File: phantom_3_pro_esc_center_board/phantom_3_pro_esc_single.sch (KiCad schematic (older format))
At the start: 103 parts

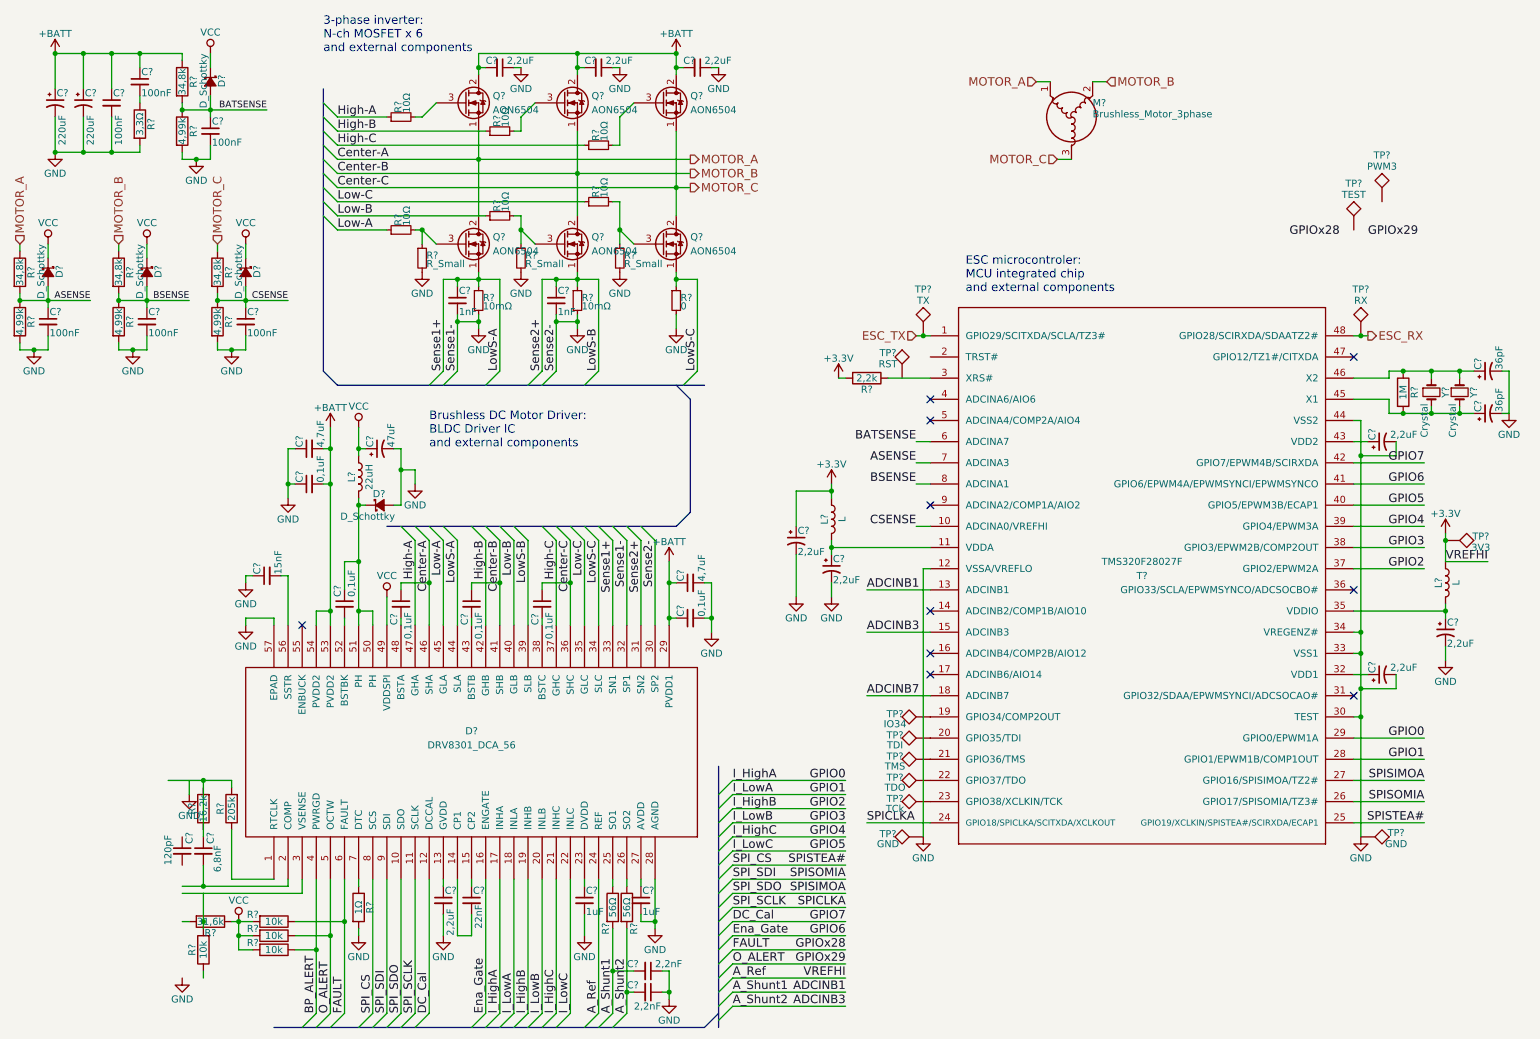
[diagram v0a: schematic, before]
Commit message: Renumbered components.
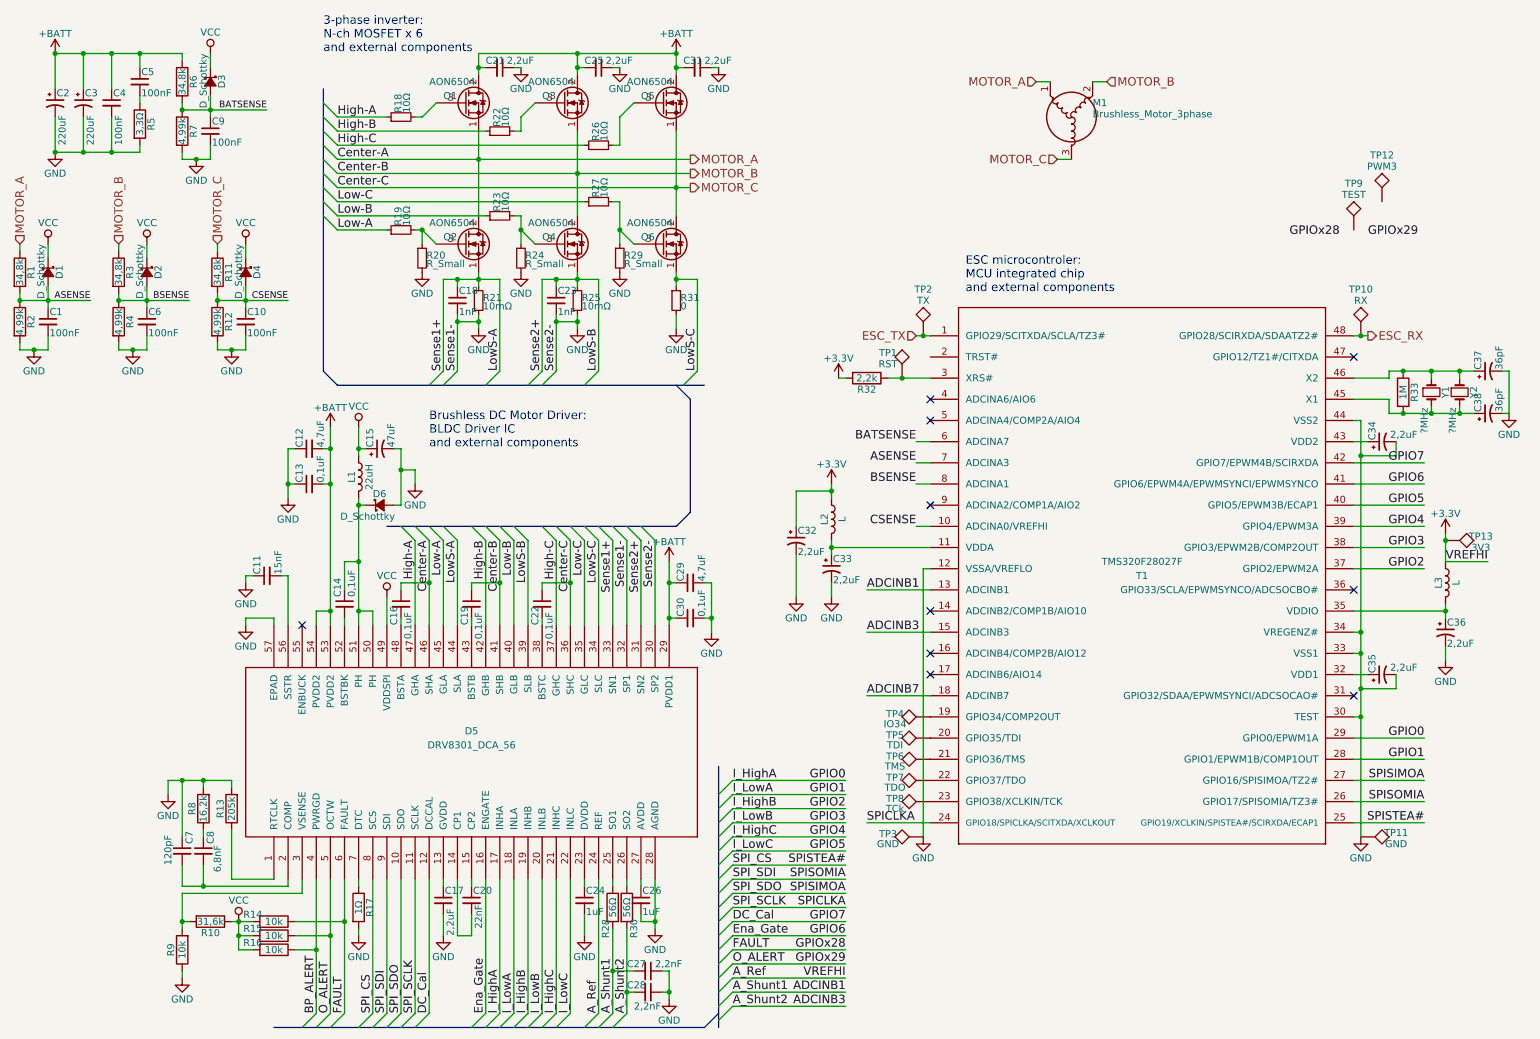
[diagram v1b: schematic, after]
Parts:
- Y3, Y4: renamed from Y?; value Crystal -> ?MHz
- gave numbers to parts that had none: 101
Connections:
- net GND: now also C45.1, R41.2, R42.1, R46.2
- net at C46.2, D11.2 (COMP): now also C45.2
- net at D11.3 (VSENSE): now also R42.2, R43.2
- net at C46.1: now also R41.1; no longer R46.2
- net at R65.1, T2.3 (XRS#): now also TP14.1
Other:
- moved on the sheet: R9

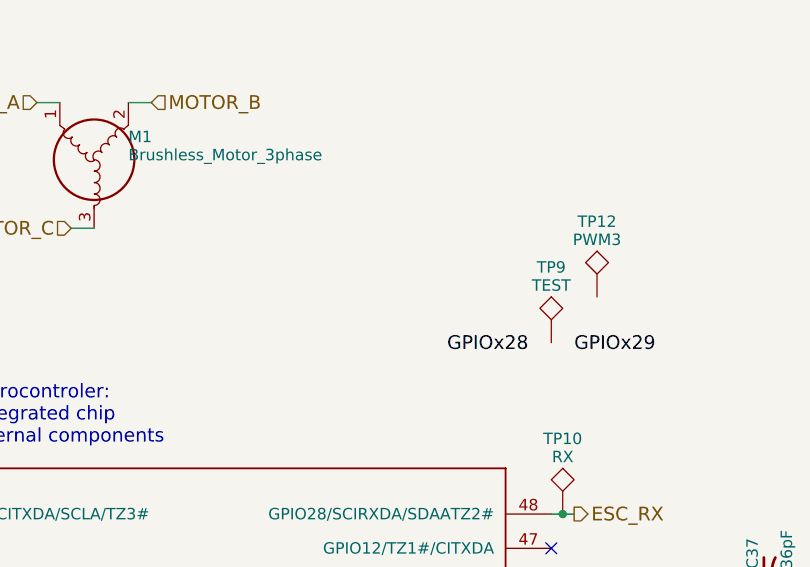
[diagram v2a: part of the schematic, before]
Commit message: ESC Center: Identified pins of FC connection.
Named all FC pins, and linked with proper connectors.
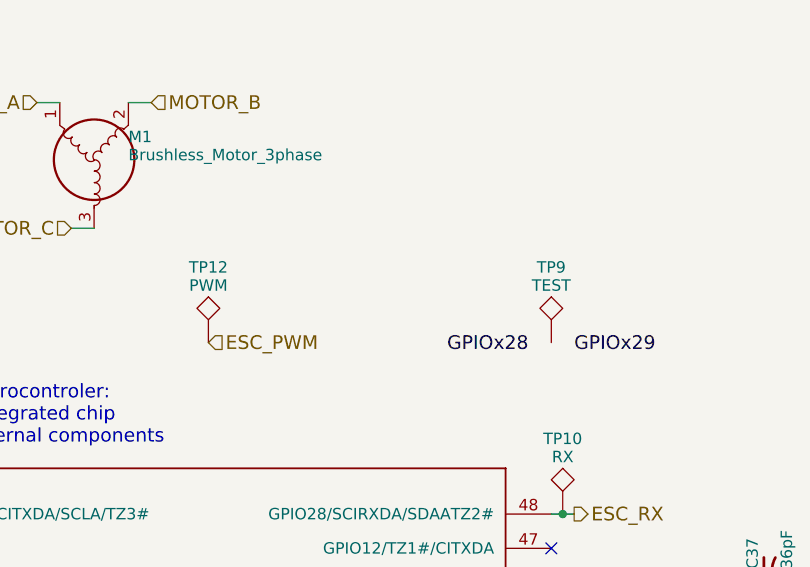
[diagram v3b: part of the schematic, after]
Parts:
- TP25: value PWM3 -> PWM
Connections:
- net ESC_PWM: now reaches TP25.1
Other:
- moved on the sheet: TP12
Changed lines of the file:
@@
 L TEST TP25
 U 1 1 590A73FE
-P 10200 1850
+P 8500 2050
 AR Path="/58FDD387/590A73FE" Ref="TP25"  Part="1"
 AR Path="/58FDAEFB/590A73FE" Ref="TP12"  Part="1"
 AR Path="/58FDDC64/590A73FE" Ref="TP38"  Part="1"
 AR Path="/58FDDC6B/590A73FE" Ref="TP51"  Part="1"
-F 0 "TP12" H 10200 2150 50  0000 C BNN
-F 1 "PWM3" H 10200 2100 50  0000 C CNN
-F 2 "" H 10200 1850 50  0001 C CNN
-F 3 "" H 10200 1850 50  0001 C CNN
-	1    10200 1850
+F 0 "TP12" H 8500 2350 50  0000 C BNN
+F 1 "PWM" H 8500 2300 50  0000 C CNN
+F 2 "" H 8500 2050 50  0001 C CNN
+F 3 "" H 8500 2050 50  0001 C CNN
+	1    8500 2050
 	1    0    0    -1
 $EndComp
@@
 	1700 6700 1700 6550
 Connection ~ 6800 3100
+Text HLabel 8500 2050 2    60   Input ~ 0
+ESC_PWM
 $EndSCHEMATC

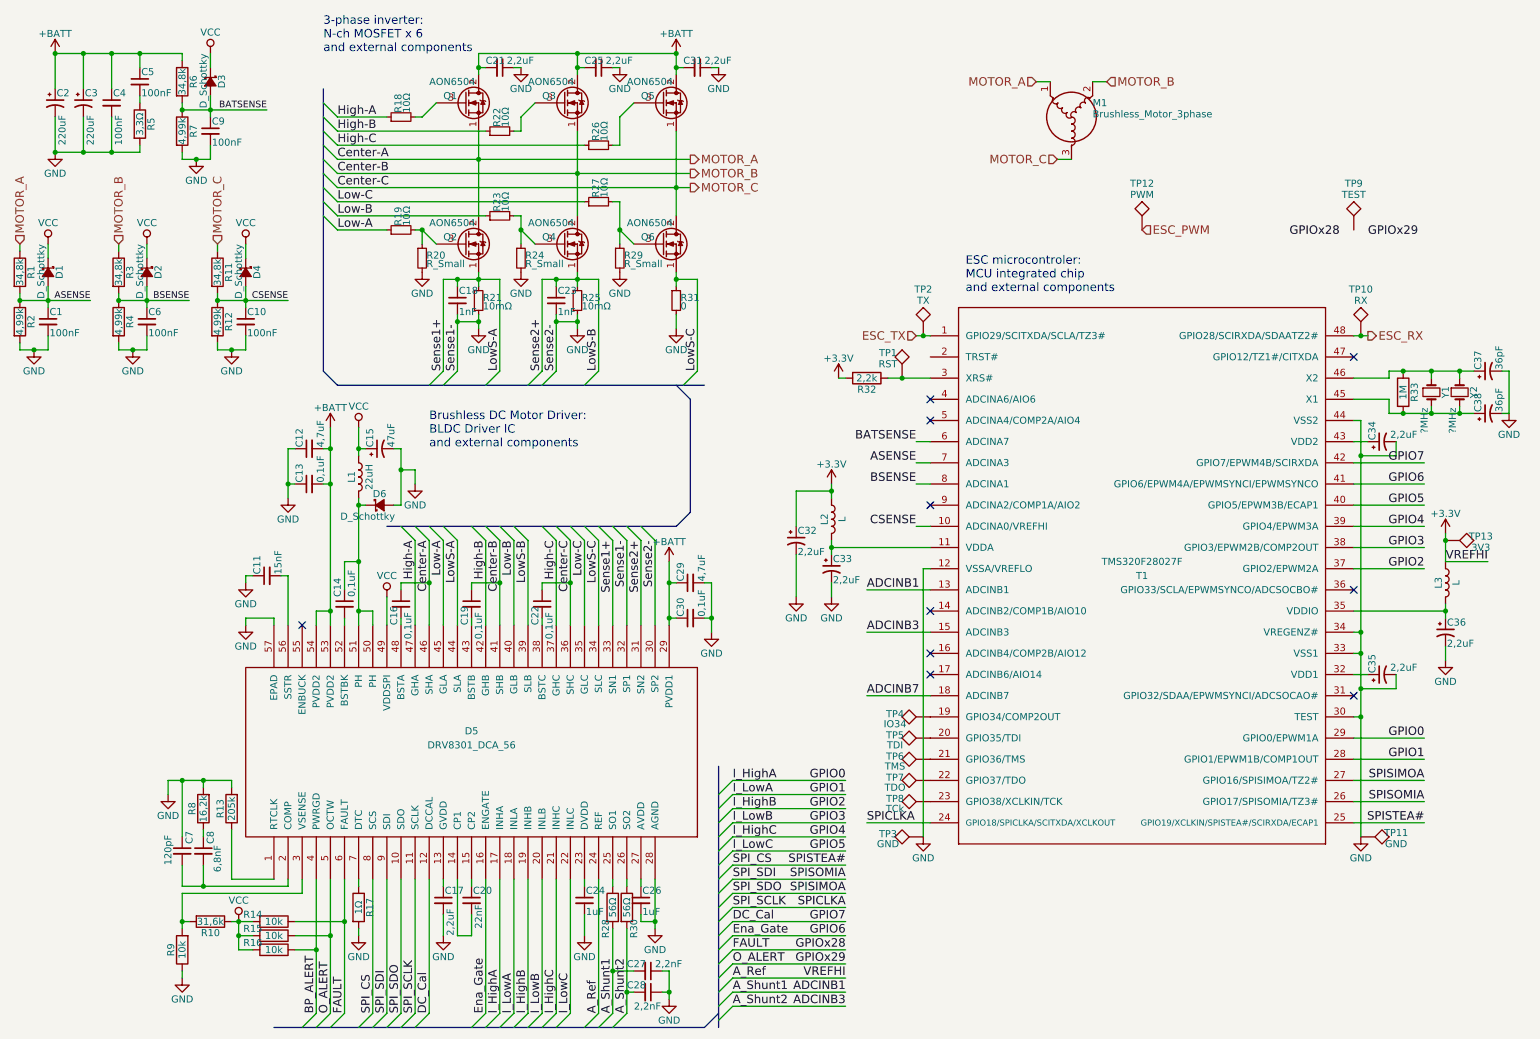
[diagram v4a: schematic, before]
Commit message: ESC Center: Updated to latest findings.
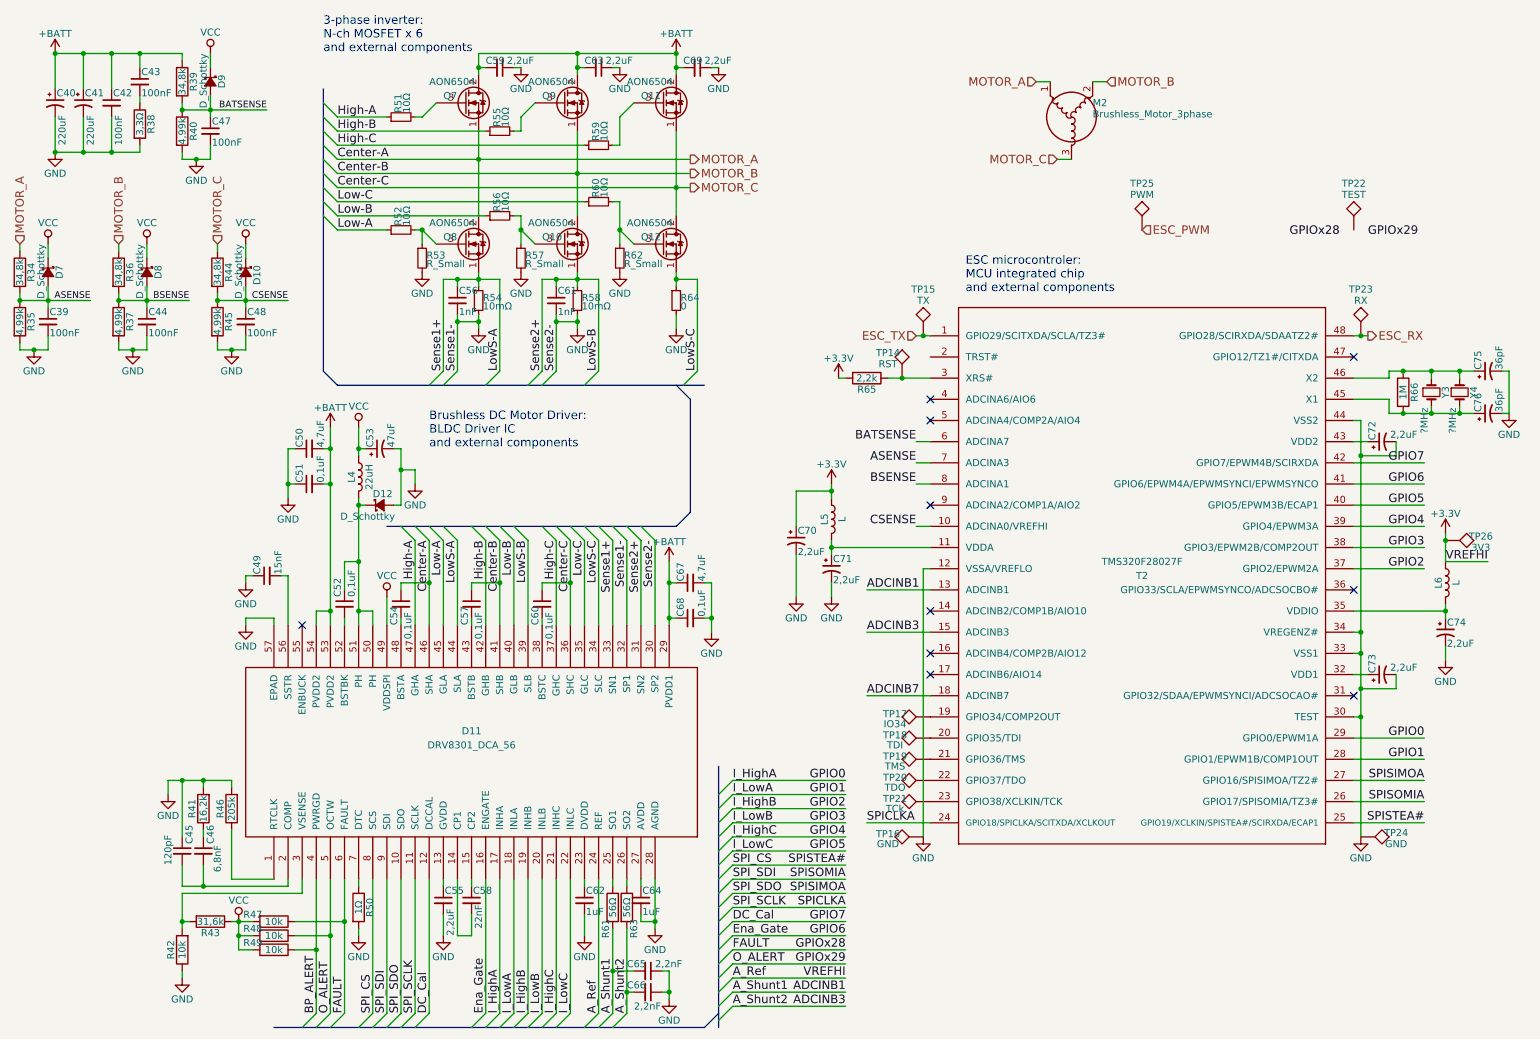
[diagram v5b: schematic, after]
